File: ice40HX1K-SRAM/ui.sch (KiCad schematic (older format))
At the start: 18 parts

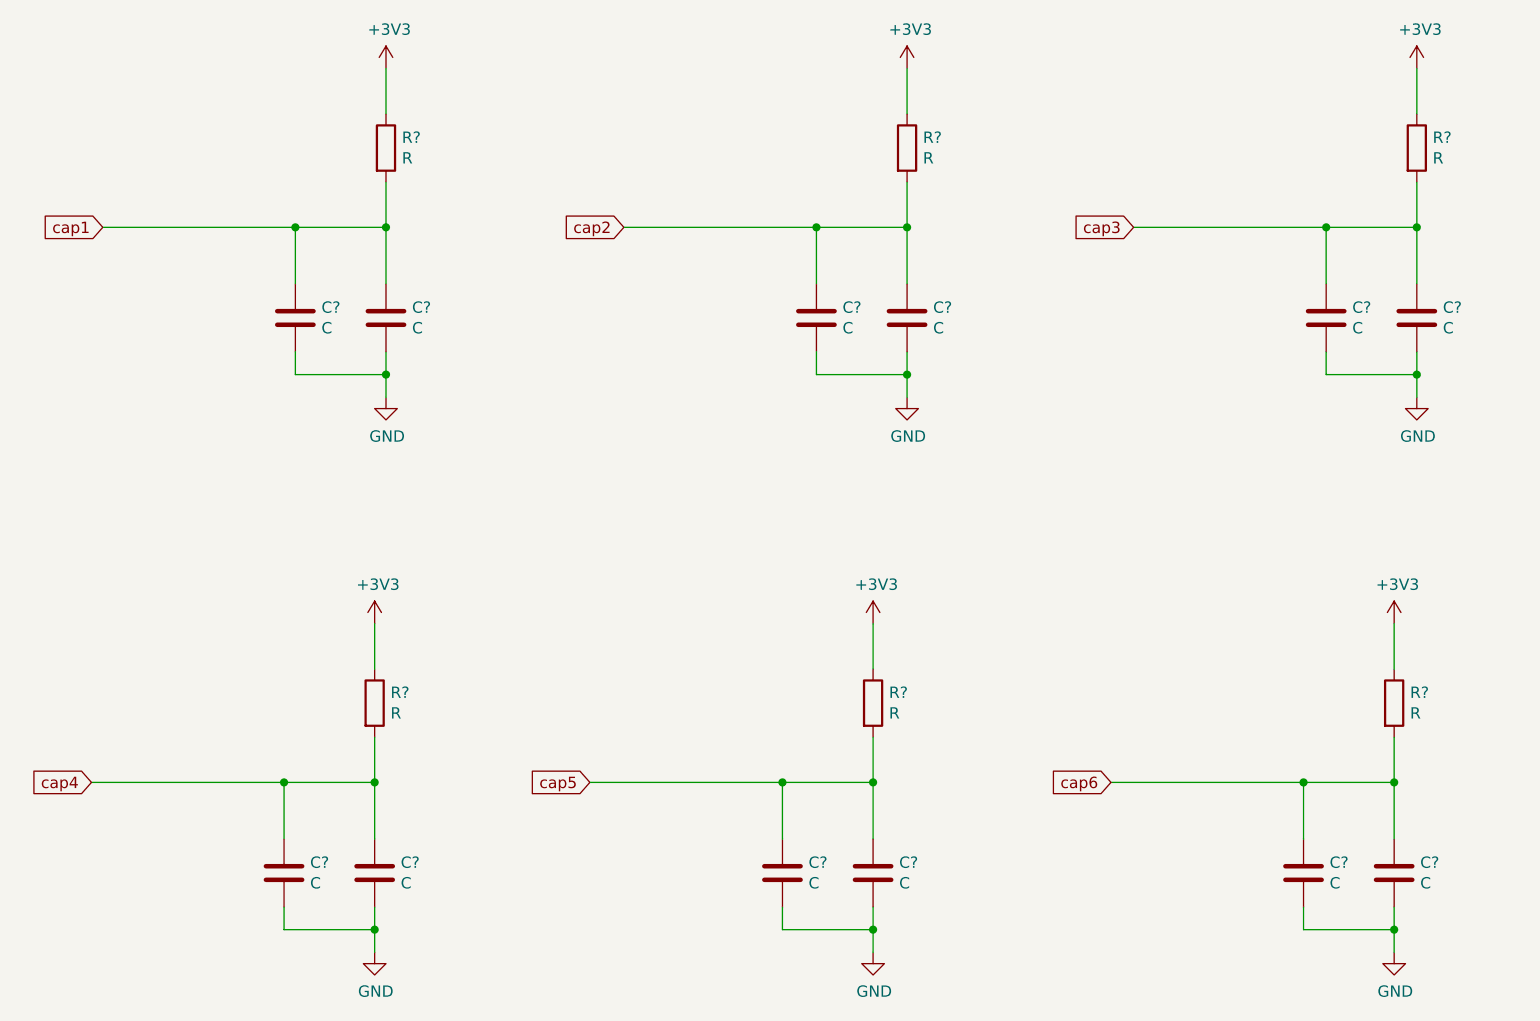
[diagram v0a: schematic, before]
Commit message: wiring FPGA nRF52 and ATSAMD11
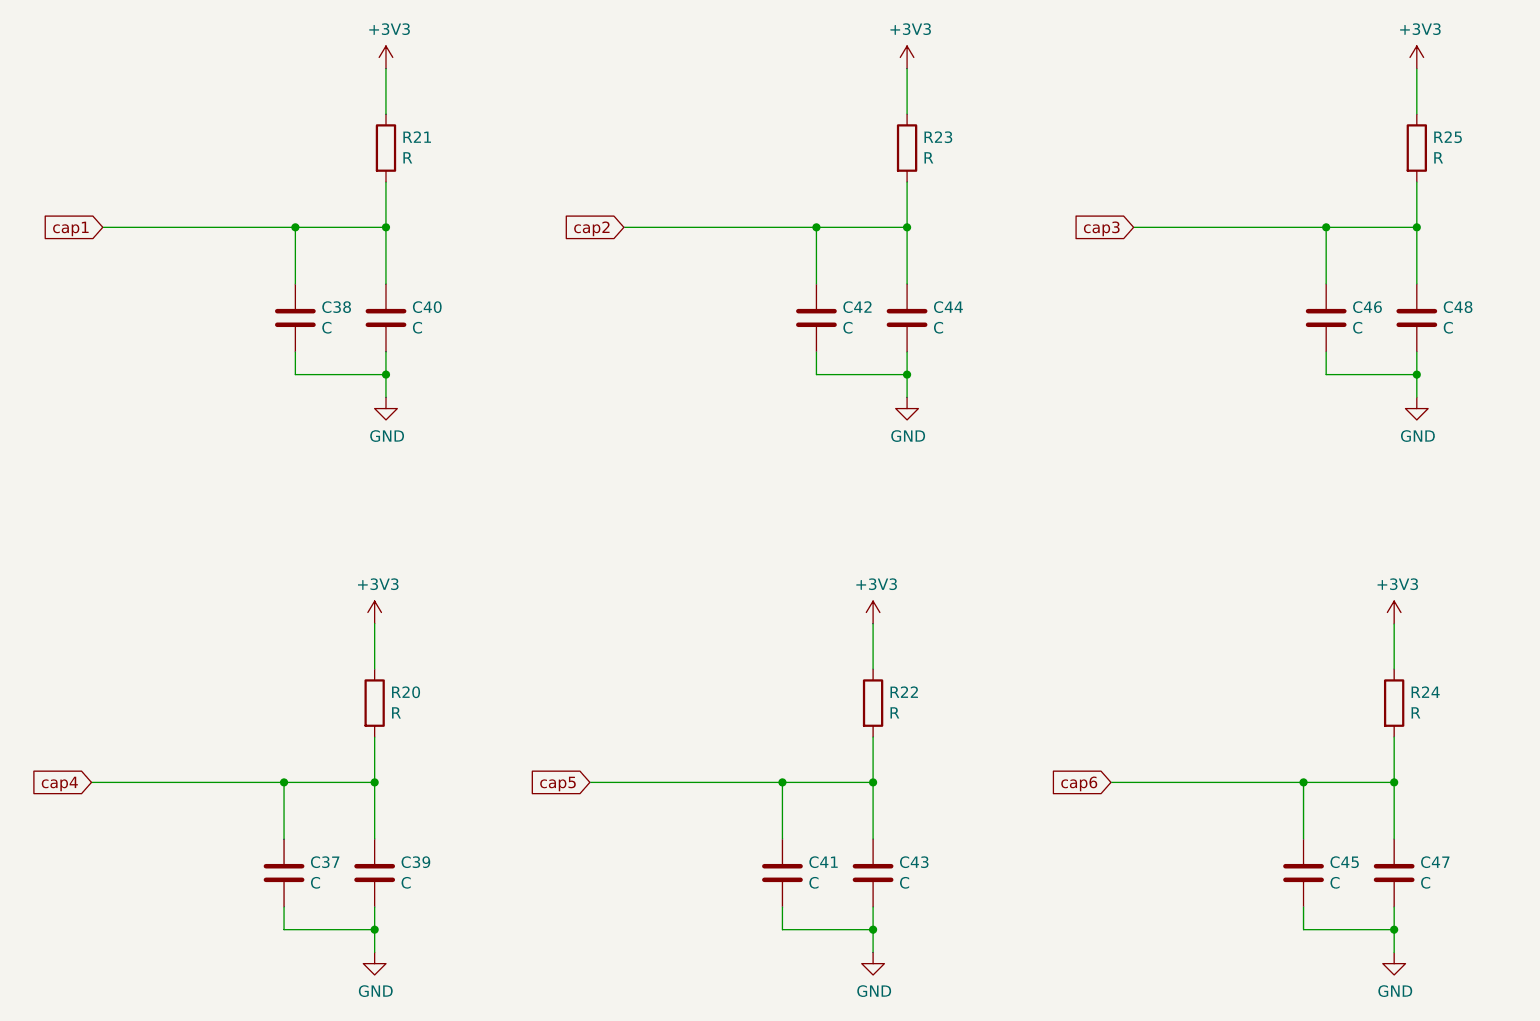
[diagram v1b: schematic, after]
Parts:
- gave numbers to parts that had none: 18
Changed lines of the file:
@@
 $EndDescr
 $Comp
-L power:GND #PWR?
+L power:GND #PWR085
 U 1 1 5E662B01
 P 2500 2400
-F 0 "#PWR?" H 2500 2150 50  0001 C CNN
+F 0 "#PWR085" H 2500 2150 50  0001 C CNN
 F 1 "GND" H 2505 2227 50  0000 C CNN
 F 2 "" H 2500 2400 50  0001 C CNN
@@
 $EndComp
 $Comp
-L power:+3V3 #PWR?
+L power:+3V3 #PWR084
 U 1 1 5E662DB1
 P 2500 950
-F 0 "#PWR?" H 2500 800 50  0001 C CNN
+F 0 "#PWR084" H 2500 800 50  0001 C CNN
 F 1 "+3V3" H 2515 1123 50  0000 C CNN
 F 2 "" H 2500 950 50  0001 C CNN
@@
 $EndComp
 $Comp
-L Device:C C?
+L Device:C C40
 U 1 1 5E662F8D
 P 2500 2050
-F 0 "C?" H 2615 2096 50  0000 L CNN
+F 0 "C40" H 2615 2096 50  0000 L CNN
 F 1 "C" H 2615 2005 50  0000 L CNN
 F 2 "" H 2538 1900 50  0001 C CNN
@@
 $EndComp
 $Comp
-L Device:C C?
+L Device:C C38
 U 1 1 5E663BB7
 P 2100 2050
-F 0 "C?" H 2215 2096 50  0000 L CNN
+F 0 "C38" H 2215 2096 50  0000 L CNN
 F 1 "C" H 2215 2005 50  0000 L CNN
 F 2 "" H 2138 1900 50  0001 C CNN
@@
 $EndComp
 $Comp
-L Device:R R?
+L Device:R R21
 U 1 1 5E663E60
 P 2500 1300
-F 0 "R?" H 2570 1346 50  0000 L CNN
+F 0 "R21" H 2570 1346 50  0000 L CNN
 F 1 "R" H 2570 1255 50  0000 L CNN
 F 2 "" V 2430 1300 50  0001 C CNN
@@
 	2100 1650 2500 1650
 $Comp
-L power:GND #PWR?
+L power:GND #PWR083
 U 1 1 5E667966
 P 2450 4850
-F 0 "#PWR?" H 2450 4600 50  0001 C CNN
+F 0 "#PWR083" H 2450 4600 50  0001 C CNN
 F 1 "GND" H 2455 4677 50  0000 C CNN
 F 2 "" H 2450 4850 50  0001 C CNN
@@
 $EndComp
 $Comp
-L power:+3V3 #PWR?
+L power:+3V3 #PWR082
 U 1 1 5E66796C
 P 2450 3400
-F 0 "#PWR?" H 2450 3250 50  0001 C CNN
+F 0 "#PWR082" H 2450 3250 50  0001 C CNN
 F 1 "+3V3" H 2465 3573 50  0000 C CNN
 F 2 "" H 2450 3400 50  0001 C CNN
@@
 $EndComp
 $Comp
-L Device:C C?
+L Device:C C39
 U 1 1 5E667972
 P 2450 4500
-F 0 "C?" H 2565 4546 50  0000 L CNN
+F 0 "C39" H 2565 4546 50  0000 L CNN
 F 1 "C" H 2565 4455 50  0000 L CNN
 F 2 "" H 2488 4350 50  0001 C CNN
@@
 $EndComp
 $Comp
-L Device:C C?
+L Device:C C37
 U 1 1 5E667978
 P 2050 4500
-F 0 "C?" H 2165 4546 50  0000 L CNN
+F 0 "C37" H 2165 4546 50  0000 L CNN
 F 1 "C" H 2165 4455 50  0000 L CNN
 F 2 "" H 2088 4350 50  0001 C CNN
@@
 $EndComp
 $Comp
-L Device:R R?
+L Device:R R20
 U 1 1 5E66797E
 P 2450 3750
-F 0 "R?" H 2520 3796 50  0000 L CNN
+F 0 "R20" H 2520 3796 50  0000 L CNN
 F 1 "R" H 2520 3705 50  0000 L CNN
 F 2 "" V 2380 3750 50  0001 C CNN
@@
 	2050 4100 2450 4100
 $Comp
-L power:GND #PWR?
+L power:GND #PWR089
 U 1 1 5E669960
 P 4800 2400
-F 0 "#PWR?" H 4800 2150 50  0001 C CNN
+F 0 "#PWR089" H 4800 2150 50  0001 C CNN
 F 1 "GND" H 4805 2227 50  0000 C CNN
 F 2 "" H 4800 2400 50  0001 C CNN
@@
 $EndComp
 $Comp
-L power:+3V3 #PWR?
+L power:+3V3 #PWR088
 U 1 1 5E669966
 P 4800 950
-F 0 "#PWR?" H 4800 800 50  0001 C CNN
+F 0 "#PWR088" H 4800 800 50  0001 C CNN
 F 1 "+3V3" H 4815 1123 50  0000 C CNN
 F 2 "" H 4800 950 50  0001 C CNN
@@
 $EndComp
 $Comp
-L Device:C C?
+L Device:C C44
 U 1 1 5E66996C
 P 4800 2050
-F 0 "C?" H 4915 2096 50  0000 L CNN
+F 0 "C44" H 4915 2096 50  0000 L CNN
 F 1 "C" H 4915 2005 50  0000 L CNN
 F 2 "" H 4838 1900 50  0001 C CNN
@@
 $EndComp
 $Comp
-L Device:C C?
+L Device:C C42
 U 1 1 5E669972
 P 4400 2050
-F 0 "C?" H 4515 2096 50  0000 L CNN
+F 0 "C42" H 4515 2096 50  0000 L CNN
 F 1 "C" H 4515 2005 50  0000 L CNN
 F 2 "" H 4438 1900 50  0001 C CNN
@@
 $EndComp
 $Comp
-L Device:R R?
+L Device:R R23
 U 1 1 5E669978
 P 4800 1300
-F 0 "R?" H 4870 1346 50  0000 L CNN
+F 0 "R23" H 4870 1346 50  0000 L CNN
 F 1 "R" H 4870 1255 50  0000 L CNN
 F 2 "" V 4730 1300 50  0001 C CNN
@@
 	4400 1650 4800 1650
 $Comp
-L power:GND #PWR?
+L power:GND #PWR087
 U 1 1 5E66BA33
 P 4650 4850
-F 0 "#PWR?" H 4650 4600 50  0001 C CNN
+F 0 "#PWR087" H 4650 4600 50  0001 C CNN
 F 1 "GND" H 4655 4677 50  0000 C CNN
 F 2 "" H 4650 4850 50  0001 C CNN
@@
 $EndComp
 $Comp
-L power:+3V3 #PWR?
+L power:+3V3 #PWR086
 U 1 1 5E66BA39
 P 4650 3400
-F 0 "#PWR?" H 4650 3250 50  0001 C CNN
+F 0 "#PWR086" H 4650 3250 50  0001 C CNN
 F 1 "+3V3" H 4665 3573 50  0000 C CNN
 F 2 "" H 4650 3400 50  0001 C CNN
@@
 $EndComp
 $Comp
-L Device:C C?
+L Device:C C43
 U 1 1 5E66BA3F
 P 4650 4500
-F 0 "C?" H 4765 4546 50  0000 L CNN
+F 0 "C43" H 4765 4546 50  0000 L CNN
 F 1 "C" H 4765 4455 50  0000 L CNN
 F 2 "" H 4688 4350 50  0001 C CNN
@@
 $EndComp
 $Comp
-L Device:C C?
+L Device:C C41
 U 1 1 5E66BA45
 P 4250 4500
-F 0 "C?" H 4365 4546 50  0000 L CNN
+F 0 "C41" H 4365 4546 50  0000 L CNN
 F 1 "C" H 4365 4455 50  0000 L CNN
 F 2 "" H 4288 4350 50  0001 C CNN
@@
 $EndComp
 $Comp
-L Device:R R?
+L Device:R R22
 U 1 1 5E66BA4B
 P 4650 3750
-F 0 "R?" H 4720 3796 50  0000 L CNN
+F 0 "R22" H 4720 3796 50  0000 L CNN
 F 1 "R" H 4720 3705 50  0000 L CNN
 F 2 "" V 4580 3750 50  0001 C CNN
@@
 	4250 4100 4650 4100
 $Comp
-L power:GND #PWR?
+L power:GND #PWR093
 U 1 1 5E66D303
 P 7050 2400
-F 0 "#PWR?" H 7050 2150 50  0001 C CNN
+F 0 "#PWR093" H 7050 2150 50  0001 C CNN
 F 1 "GND" H 7055 2227 50  0000 C CNN
 F 2 "" H 7050 2400 50  0001 C CNN
@@
 $EndComp
 $Comp
-L power:+3V3 #PWR?
+L power:+3V3 #PWR092
 U 1 1 5E66D309
 P 7050 950
-F 0 "#PWR?" H 7050 800 50  0001 C CNN
+F 0 "#PWR092" H 7050 800 50  0001 C CNN
 F 1 "+3V3" H 7065 1123 50  0000 C CNN
 F 2 "" H 7050 950 50  0001 C CNN
@@
 $EndComp
 $Comp
-L Device:C C?
+L Device:C C48
 U 1 1 5E66D30F
 P 7050 2050
-F 0 "C?" H 7165 2096 50  0000 L CNN
+F 0 "C48" H 7165 2096 50  0000 L CNN
 F 1 "C" H 7165 2005 50  0000 L CNN
 F 2 "" H 7088 1900 50  0001 C CNN
@@
 $EndComp
 $Comp
-L Device:C C?
+L Device:C C46
 U 1 1 5E66D315
 P 6650 2050
-F 0 "C?" H 6765 2096 50  0000 L CNN
+F 0 "C46" H 6765 2096 50  0000 L CNN
 F 1 "C" H 6765 2005 50  0000 L CNN
 F 2 "" H 6688 1900 50  0001 C CNN
@@
 $EndComp
 $Comp
-L Device:R R?
+L Device:R R25
 U 1 1 5E66D31B
 P 7050 1300
-F 0 "R?" H 7120 1346 50  0000 L CNN
+F 0 "R25" H 7120 1346 50  0000 L CNN
 F 1 "R" H 7120 1255 50  0000 L CNN
 F 2 "" V 6980 1300 50  0001 C CNN
@@
 	6650 1650 7050 1650
 $Comp
-L power:GND #PWR?
+L power:GND #PWR091
 U 1 1 5E66F629
 P 6950 4850
-F 0 "#PWR?" H 6950 4600 50  0001 C CNN
+F 0 "#PWR091" H 6950 4600 50  0001 C CNN
 F 1 "GND" H 6955 4677 50  0000 C CNN
 F 2 "" H 6950 4850 50  0001 C CNN
@@
 $EndComp
 $Comp
-L power:+3V3 #PWR?
+L power:+3V3 #PWR090
 U 1 1 5E66F62F
 P 6950 3400
-F 0 "#PWR?" H 6950 3250 50  0001 C CNN
+F 0 "#PWR090" H 6950 3250 50  0001 C CNN
 F 1 "+3V3" H 6965 3573 50  0000 C CNN
 F 2 "" H 6950 3400 50  0001 C CNN
@@
 $EndComp
 $Comp
-L Device:C C?
+L Device:C C47
 U 1 1 5E66F635
 P 6950 4500
-F 0 "C?" H 7065 4546 50  0000 L CNN
+F 0 "C47" H 7065 4546 50  0000 L CNN
 F 1 "C" H 7065 4455 50  0000 L CNN
 F 2 "" H 6988 4350 50  0001 C CNN
@@
 $EndComp
 $Comp
-L Device:C C?
+L Device:C C45
 U 1 1 5E66F63B
 P 6550 4500
-F 0 "C?" H 6665 4546 50  0000 L CNN
+F 0 "C45" H 6665 4546 50  0000 L CNN
 F 1 "C" H 6665 4455 50  0000 L CNN
 F 2 "" H 6588 4350 50  0001 C CNN
@@
 $EndComp
 $Comp
-L Device:R R?
+L Device:R R24
 U 1 1 5E66F641
 P 6950 3750
-F 0 "R?" H 7020 3796 50  0000 L CNN
+F 0 "R24" H 7020 3796 50  0000 L CNN
 F 1 "R" H 7020 3705 50  0000 L CNN
 F 2 "" V 6880 3750 50  0001 C CNN

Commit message: wiring FPGA
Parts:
- C37, C38: value C -> 100pF; footprint (none) -> Capacitor_SMD:C_0402_1005Metric
- C39, C40, C43, C44, C47, C48: value C -> Ccap
- C41, C42, C45, C46: value C -> 100pF
- R20, R21, R22, R23, R24, R25: value R -> 100kOhm; footprint (none) -> Resistor_SMD:R_0402_1005Metric
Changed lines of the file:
@@
 P 2500 2050
 F 0 "C40" H 2615 2096 50  0000 L CNN
-F 1 "C" H 2615 2005 50  0000 L CNN
+F 1 "Ccap" H 2615 2005 50  0000 L CNN
 F 2 "" H 2538 1900 50  0001 C CNN
 F 3 "~" H 2500 2050 50  0001 C CNN
@@
 P 2100 2050
 F 0 "C38" H 2215 2096 50  0000 L CNN
-F 1 "C" H 2215 2005 50  0000 L CNN
-F 2 "" H 2138 1900 50  0001 C CNN
+F 1 "100pF" H 2215 2005 50  0000 L CNN
+F 2 "Capacitor_SMD:C_0402_1005Metric" H 2138 1900 50  0001 C CNN
 F 3 "~" H 2100 2050 50  0001 C CNN
 	1    2100 2050
@@
 P 2500 1300
 F 0 "R21" H 2570 1346 50  0000 L CNN
-F 1 "R" H 2570 1255 50  0000 L CNN
-F 2 "" V 2430 1300 50  0001 C CNN
+F 1 "100kOhm" H 2570 1255 50  0000 L CNN
+F 2 "Resistor_SMD:R_0402_1005Metric" V 2430 1300 50  0001 C CNN
 F 3 "~" H 2500 1300 50  0001 C CNN
 	1    2500 1300
@@
 P 2450 4500
 F 0 "C39" H 2565 4546 50  0000 L CNN
-F 1 "C" H 2565 4455 50  0000 L CNN
+F 1 "Ccap" H 2565 4455 50  0000 L CNN
 F 2 "" H 2488 4350 50  0001 C CNN
 F 3 "~" H 2450 4500 50  0001 C CNN
@@
 P 2050 4500
 F 0 "C37" H 2165 4546 50  0000 L CNN
-F 1 "C" H 2165 4455 50  0000 L CNN
-F 2 "" H 2088 4350 50  0001 C CNN
+F 1 "100pF" H 2165 4455 50  0000 L CNN
+F 2 "Capacitor_SMD:C_0402_1005Metric" H 2088 4350 50  0001 C CNN
 F 3 "~" H 2050 4500 50  0001 C CNN
 	1    2050 4500
@@
 P 2450 3750
 F 0 "R20" H 2520 3796 50  0000 L CNN
-F 1 "R" H 2520 3705 50  0000 L CNN
-F 2 "" V 2380 3750 50  0001 C CNN
+F 1 "100kOhm" H 2520 3705 50  0000 L CNN
+F 2 "Resistor_SMD:R_0402_1005Metric" V 2380 3750 50  0001 C CNN
 F 3 "~" H 2450 3750 50  0001 C CNN
 	1    2450 3750
@@
 P 4800 2050
 F 0 "C44" H 4915 2096 50  0000 L CNN
-F 1 "C" H 4915 2005 50  0000 L CNN
+F 1 "Ccap" H 4915 2005 50  0000 L CNN
 F 2 "" H 4838 1900 50  0001 C CNN
 F 3 "~" H 4800 2050 50  0001 C CNN
@@
 P 4400 2050
 F 0 "C42" H 4515 2096 50  0000 L CNN
-F 1 "C" H 4515 2005 50  0000 L CNN
+F 1 "100pF" H 4515 2005 50  0000 L CNN
 F 2 "" H 4438 1900 50  0001 C CNN
 F 3 "~" H 4400 2050 50  0001 C CNN
@@
 P 4800 1300
 F 0 "R23" H 4870 1346 50  0000 L CNN
-F 1 "R" H 4870 1255 50  0000 L CNN
-F 2 "" V 4730 1300 50  0001 C CNN
+F 1 "100kOhm" H 4870 1255 50  0000 L CNN
+F 2 "Resistor_SMD:R_0402_1005Metric" V 4730 1300 50  0001 C CNN
 F 3 "~" H 4800 1300 50  0001 C CNN
 	1    4800 1300
@@
 P 4650 4500
 F 0 "C43" H 4765 4546 50  0000 L CNN
-F 1 "C" H 4765 4455 50  0000 L CNN
+F 1 "Ccap" H 4765 4455 50  0000 L CNN
 F 2 "" H 4688 4350 50  0001 C CNN
 F 3 "~" H 4650 4500 50  0001 C CNN
@@
 P 4250 4500
 F 0 "C41" H 4365 4546 50  0000 L CNN
-F 1 "C" H 4365 4455 50  0000 L CNN
+F 1 "100pF" H 4365 4455 50  0000 L CNN
 F 2 "" H 4288 4350 50  0001 C CNN
 F 3 "~" H 4250 4500 50  0001 C CNN
@@
 P 4650 3750
 F 0 "R22" H 4720 3796 50  0000 L CNN
-F 1 "R" H 4720 3705 50  0000 L CNN
-F 2 "" V 4580 3750 50  0001 C CNN
+F 1 "100kOhm" H 4720 3705 50  0000 L CNN
+F 2 "Resistor_SMD:R_0402_1005Metric" V 4580 3750 50  0001 C CNN
 F 3 "~" H 4650 3750 50  0001 C CNN
 	1    4650 3750
@@
 P 7050 2050
 F 0 "C48" H 7165 2096 50  0000 L CNN
-F 1 "C" H 7165 2005 50  0000 L CNN
+F 1 "Ccap" H 7165 2005 50  0000 L CNN
 F 2 "" H 7088 1900 50  0001 C CNN
 F 3 "~" H 7050 2050 50  0001 C CNN
@@
 P 6650 2050
 F 0 "C46" H 6765 2096 50  0000 L CNN
-F 1 "C" H 6765 2005 50  0000 L CNN
+F 1 "100pF" H 6765 2005 50  0000 L CNN
 F 2 "" H 6688 1900 50  0001 C CNN
 F 3 "~" H 6650 2050 50  0001 C CNN
@@
 P 7050 1300
 F 0 "R25" H 7120 1346 50  0000 L CNN
-F 1 "R" H 7120 1255 50  0000 L CNN
-F 2 "" V 6980 1300 50  0001 C CNN
+F 1 "100kOhm" H 7120 1255 50  0000 L CNN
+F 2 "Resistor_SMD:R_0402_1005Metric" V 6980 1300 50  0001 C CNN
 F 3 "~" H 7050 1300 50  0001 C CNN
 	1    7050 1300
@@
 P 6950 4500
 F 0 "C47" H 7065 4546 50  0000 L CNN
-F 1 "C" H 7065 4455 50  0000 L CNN
+F 1 "Ccap" H 7065 4455 50  0000 L CNN
 F 2 "" H 6988 4350 50  0001 C CNN
 F 3 "~" H 6950 4500 50  0001 C CNN
@@
 P 6550 4500
 F 0 "C45" H 6665 4546 50  0000 L CNN
-F 1 "C" H 6665 4455 50  0000 L CNN
+F 1 "100pF" H 6665 4455 50  0000 L CNN
 F 2 "" H 6588 4350 50  0001 C CNN
 F 3 "~" H 6550 4500 50  0001 C CNN
@@
 P 6950 3750
 F 0 "R24" H 7020 3796 50  0000 L CNN
-F 1 "R" H 7020 3705 50  0000 L CNN
-F 2 "" V 6880 3750 50  0001 C CNN
+F 1 "100kOhm" H 7020 3705 50  0000 L CNN
+F 2 "Resistor_SMD:R_0402_1005Metric" V 6880 3750 50  0001 C CNN
 F 3 "~" H 6950 3750 50  0001 C CNN
 	1    6950 3750

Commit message: starting layout
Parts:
- C39, C40, C43, C44, C47, C48: footprint (none) -> kifootp:CAPBUTTON
- C41, C42, C45, C46: footprint (none) -> Capacitor_SMD:C_0402_1005Metric
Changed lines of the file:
@@
 F 0 "C40" H 2615 2096 50  0000 L CNN
 F 1 "Ccap" H 2615 2005 50  0000 L CNN
-F 2 "" H 2538 1900 50  0001 C CNN
+F 2 "kifootp:CAPBUTTON" H 2538 1900 50  0001 C CNN
 F 3 "~" H 2500 2050 50  0001 C CNN
 	1    2500 2050
@@
 F 0 "C39" H 2565 4546 50  0000 L CNN
 F 1 "Ccap" H 2565 4455 50  0000 L CNN
-F 2 "" H 2488 4350 50  0001 C CNN
+F 2 "kifootp:CAPBUTTON" H 2488 4350 50  0001 C CNN
 F 3 "~" H 2450 4500 50  0001 C CNN
 	1    2450 4500
@@
 F 0 "C44" H 4915 2096 50  0000 L CNN
 F 1 "Ccap" H 4915 2005 50  0000 L CNN
-F 2 "" H 4838 1900 50  0001 C CNN
+F 2 "kifootp:CAPBUTTON" H 4838 1900 50  0001 C CNN
 F 3 "~" H 4800 2050 50  0001 C CNN
 	1    4800 2050
@@
 F 0 "C42" H 4515 2096 50  0000 L CNN
 F 1 "100pF" H 4515 2005 50  0000 L CNN
-F 2 "" H 4438 1900 50  0001 C CNN
+F 2 "Capacitor_SMD:C_0402_1005Metric" H 4438 1900 50  0001 C CNN
 F 3 "~" H 4400 2050 50  0001 C CNN
 	1    4400 2050
@@
 F 0 "C43" H 4765 4546 50  0000 L CNN
 F 1 "Ccap" H 4765 4455 50  0000 L CNN
-F 2 "" H 4688 4350 50  0001 C CNN
+F 2 "kifootp:CAPBUTTON" H 4688 4350 50  0001 C CNN
 F 3 "~" H 4650 4500 50  0001 C CNN
 	1    4650 4500
@@
 F 0 "C41" H 4365 4546 50  0000 L CNN
 F 1 "100pF" H 4365 4455 50  0000 L CNN
-F 2 "" H 4288 4350 50  0001 C CNN
+F 2 "Capacitor_SMD:C_0402_1005Metric" H 4288 4350 50  0001 C CNN
 F 3 "~" H 4250 4500 50  0001 C CNN
 	1    4250 4500
@@
 F 0 "C48" H 7165 2096 50  0000 L CNN
 F 1 "Ccap" H 7165 2005 50  0000 L CNN
-F 2 "" H 7088 1900 50  0001 C CNN
+F 2 "kifootp:CAPBUTTON" H 7088 1900 50  0001 C CNN
 F 3 "~" H 7050 2050 50  0001 C CNN
 	1    7050 2050
@@
 F 0 "C46" H 6765 2096 50  0000 L CNN
 F 1 "100pF" H 6765 2005 50  0000 L CNN
-F 2 "" H 6688 1900 50  0001 C CNN
+F 2 "Capacitor_SMD:C_0402_1005Metric" H 6688 1900 50  0001 C CNN
 F 3 "~" H 6650 2050 50  0001 C CNN
 	1    6650 2050
@@
 F 0 "C47" H 7065 4546 50  0000 L CNN
 F 1 "Ccap" H 7065 4455 50  0000 L CNN
-F 2 "" H 6988 4350 50  0001 C CNN
+F 2 "kifootp:CAPBUTTON" H 6988 4350 50  0001 C CNN
 F 3 "~" H 6950 4500 50  0001 C CNN
 	1    6950 4500
@@
 F 0 "C45" H 6665 4546 50  0000 L CNN
 F 1 "100pF" H 6665 4455 50  0000 L CNN
-F 2 "" H 6588 4350 50  0001 C CNN
+F 2 "Capacitor_SMD:C_0402_1005Metric" H 6588 4350 50  0001 C CNN
 F 3 "~" H 6550 4500 50  0001 C CNN
 	1    6550 4500
